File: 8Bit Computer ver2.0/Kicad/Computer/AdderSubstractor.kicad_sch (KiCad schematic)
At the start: 15 parts, among them IC140 SN74AHC74DR, IC141 SN74HCS4075DR, IC142 SN74LVC1G32DBVR, IC143 SN74AHC86DR, IC144 SN74LVC1G08DBVR, IC145 SN74LVC1G14DBVR, IC146 SN74AHC86DR, IC147 SN74ABT245BDWR, IC148 SN74F283D, IC149 SN74F283D, IC150 SN74F283D, IC151 SN74LVC1G86DBVR, IC152 SN74ABT574ADWR, IC153 SN74ABT574ADWR, IC154 SN74LVC1G14DBVR

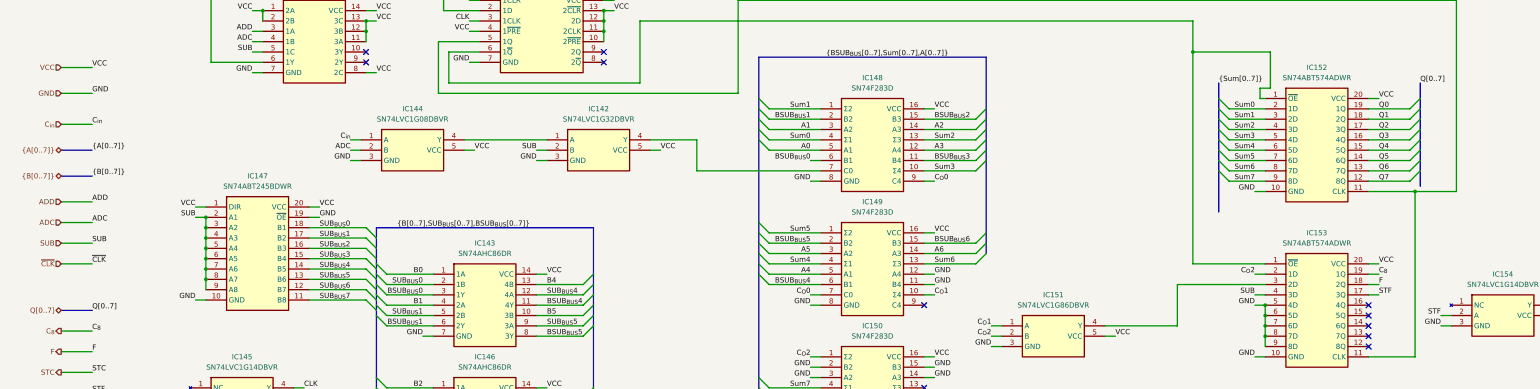
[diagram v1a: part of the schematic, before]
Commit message: Kicad, parts
Parts:
added Leds
Kicad:
added Input Output
changed Q bus to DAT bus
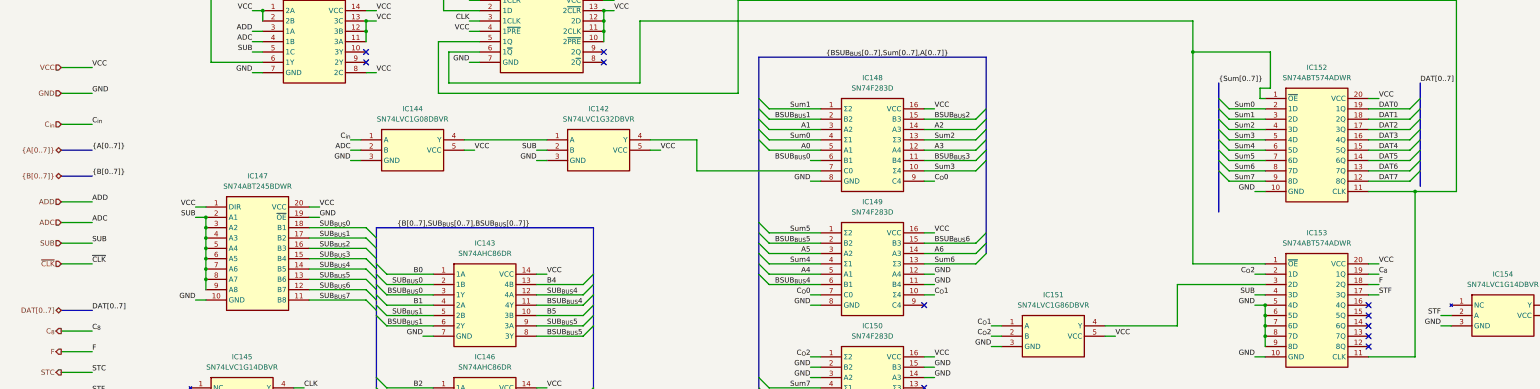
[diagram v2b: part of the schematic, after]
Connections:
- net Q0 renamed DAT0
- net Q1 renamed DAT1
- net Q2 renamed DAT2
- net Q3 renamed DAT3
- net Q4 renamed DAT4
- net Q5 renamed DAT5
- net Q6 renamed DAT6
- net Q7 renamed DAT7
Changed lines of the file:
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@@
 		)
 	)
-	(label "Q2"
+	(label "DAT2"
 		(at 355.6 64.77 0)
 		(effects
@@
 		)
 	)
-	(label "Q[0..7]"
+	(label "DAT[0..7]"
 		(at 39.37 109.22 0)
 		(effects
@@
 		)
 	)
-	(label "Q3"
+	(label "DAT3"
 		(at 355.6 67.31 0)
 		(effects
@@
 		)
 	)
-	(label "Q4"
+	(label "DAT4"
 		(at 355.6 69.85 0)
 		(effects
@@
 		)
 	)
-	(label "Q5"
+	(label "DAT5"
 		(at 355.6 72.39 0)
 		(effects
@@
 		)
 	)
-	(label "Q1"
+	(label "DAT1"
 		(at 355.6 62.23 0)
 		(effects
@@
 		)
 	)
-	(label "Q6"
+	(label "DAT6"
 		(at 355.6 74.93 0)
 		(effects
@@
 		)
 	)
-	(label "Q0"
+	(label "DAT0"
 		(at 355.6 59.69 0)
 		(effects
@@
 		)
 	)
-	(label "Q[0..7]"
+	(label "DAT[0..7]"
 		(at 365.76 53.34 0)
 		(effects
@@
 		)
 	)
-	(label "Q7"
+	(label "DAT7"
 		(at 355.6 77.47 0)
 		(effects
@@
 		)
 	)
-	(hierarchical_label "Q[0..7]"
+	(hierarchical_label "DAT[0..7]"
 		(shape tri_state)
 		(at 31.75 109.22 180)

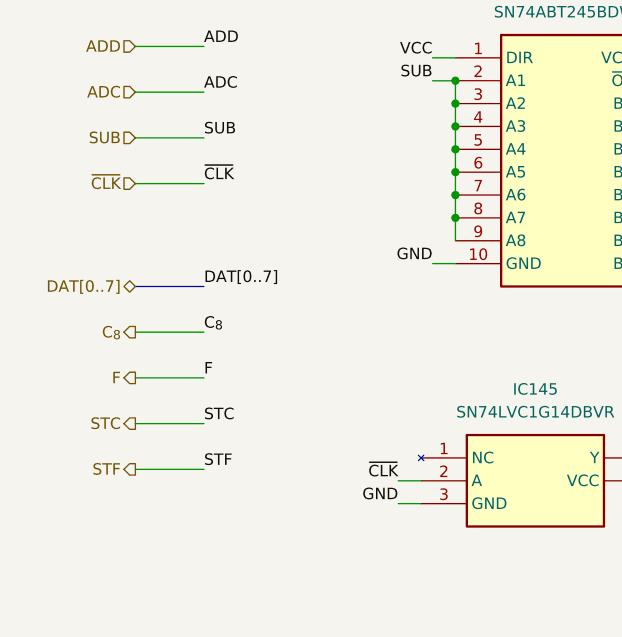
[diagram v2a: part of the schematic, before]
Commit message: Kicad, parts
parts:
added USB C PD Triggerboard
added Delay Chip for 90ns
added Push Button
Kicad:
added USB C PD Triggerboard
added rising edge detector via Delay and Xor for Accept Push Button
added VBUS net
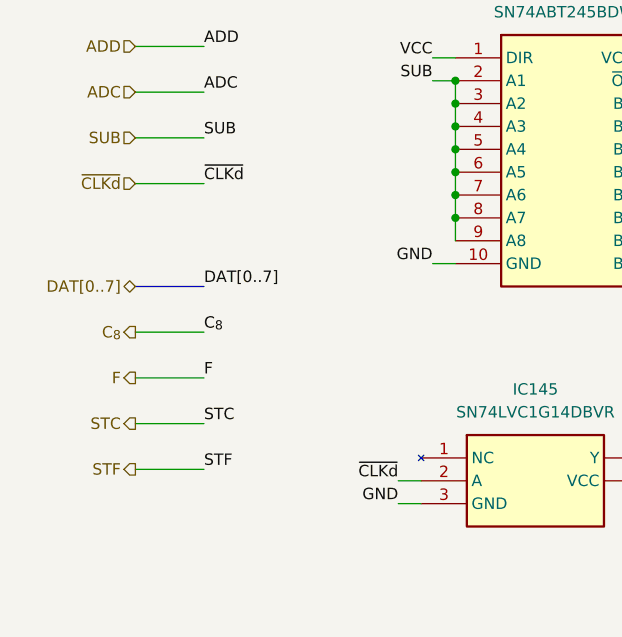
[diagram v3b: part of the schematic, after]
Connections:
- net ~{CLK} renamed ~{CLKd}
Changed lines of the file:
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@@
 		)
 	)
-	(label "~{CLK}"
+	(label "~{CLKd}"
 		(at 39.37 97.79 0)
 		(effects
@@
 		)
 	)
-	(label "~{CLK}"
+	(label "~{CLKd}"
 		(at 60.96 130.81 180)
 		(effects
@@
 		)
 	)
-	(hierarchical_label "~{CLK}"
+	(hierarchical_label "~{CLKd}"
 		(shape input)
 		(at 31.75 97.79 180)

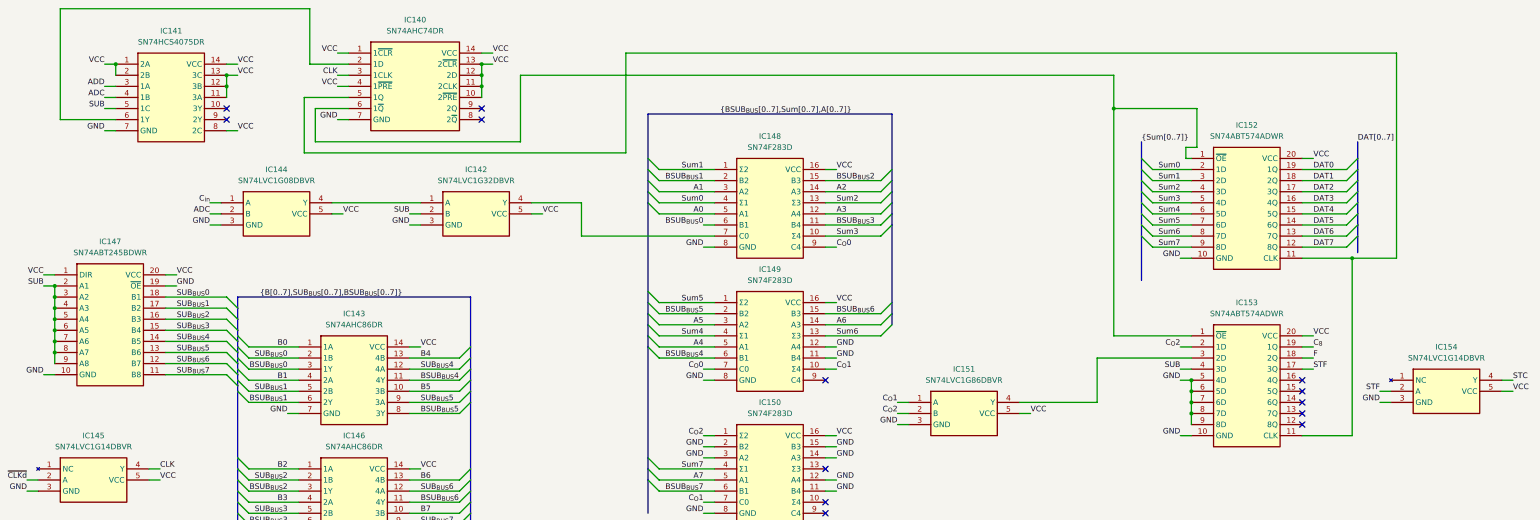
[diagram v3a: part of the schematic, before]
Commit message: Kicad SCH/PCB
Kicad SCH/PCB:
changed the References in SCH
began with INOUTPUT module nearly done
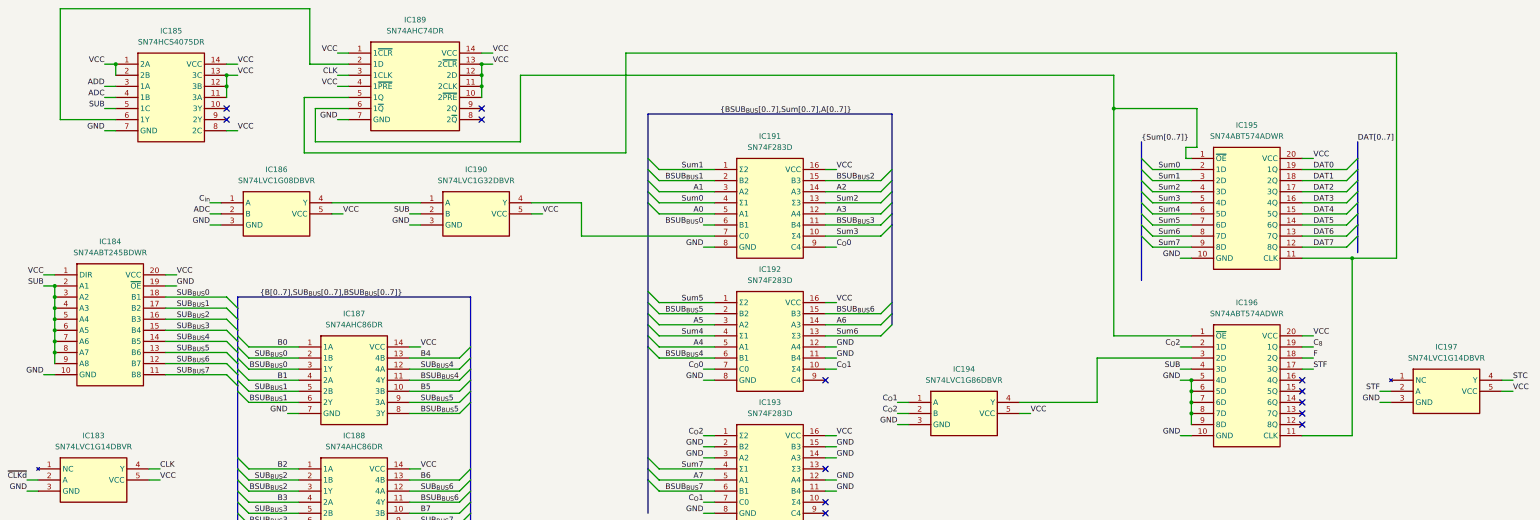
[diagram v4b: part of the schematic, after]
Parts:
- renumbered IC145 to IC183, IC147 to IC184, IC141 to IC185, IC144 to IC186, IC143 to IC187, IC146 to IC188, IC140 to IC189, IC142 to IC190, IC148 to IC191, IC149 to IC192, IC150 to IC193, IC151 to IC194, IC152 to IC195, IC153 to IC196, IC154 to IC197
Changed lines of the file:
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@@
 		(dnp no)
 		(fields_autoplaced yes)
-		(property "Reference" "IC147"
+		(property "Reference" "IC184"
 			(at 80.01 76.2 0)
 			(effects
@@
 			(project ""
 				(path "/1196a00e-6878-4d6d-82b7-9e052dfe7c14/c4d8b530-1c6d-45af-88d2-7dc1d4321a34/fab3b598-6285-4b88-9c97-383a6e59f4fc"
-					(reference "IC147")
+					(reference "IC184")
 					(unit 1)
 				)
@@
 		(dnp no)
 		(fields_autoplaced yes)
-		(property "Reference" "IC146"
+		(property "Reference" "IC188"
 			(at 135.89 120.65 0)
 			(effects
@@
 			(project "Computer"
 				(path "/1196a00e-6878-4d6d-82b7-9e052dfe7c14/c4d8b530-1c6d-45af-88d2-7dc1d4321a34/fab3b598-6285-4b88-9c97-383a6e59f4fc"
-					(reference "IC146")
+					(reference "IC188")
 					(unit 1)
 				)
@@
 		(dnp no)
 		(fields_autoplaced yes)
-		(property "Reference" "IC152"
+		(property "Reference" "IC195"
 			(at 340.36 49.53 0)
 			(effects
@@
 			(project "Computer"
 				(path "/1196a00e-6878-4d6d-82b7-9e052dfe7c14/c4d8b530-1c6d-45af-88d2-7dc1d4321a34/fab3b598-6285-4b88-9c97-383a6e59f4fc"
-					(reference "IC152")
+					(reference "IC195")
 					(unit 1)
 				)
@@
 		(dnp no)
 		(fields_autoplaced yes)
-		(property "Reference" "IC153"
+		(property "Reference" "IC196"
 			(at 340.36 90.17 0)
 			(effects
@@
 			(project "Computer"
 				(path "/1196a00e-6878-4d6d-82b7-9e052dfe7c14/c4d8b530-1c6d-45af-88d2-7dc1d4321a34/fab3b598-6285-4b88-9c97-383a6e59f4fc"
-					(reference "IC153")
+					(reference "IC196")
 					(unit 1)
 				)
@@
 		(dnp no)
 		(fields_autoplaced yes)
-		(property "Reference" "IC145"
+		(property "Reference" "IC183"
 			(at 76.2 120.65 0)
 			(effects
@@
 			(project ""
 				(path "/1196a00e-6878-4d6d-82b7-9e052dfe7c14/c4d8b530-1c6d-45af-88d2-7dc1d4321a34/fab3b598-6285-4b88-9c97-383a6e59f4fc"
-					(reference "IC145")
+					(reference "IC183")
 					(unit 1)
 				)
@@
 		(dnp no)
 		(fields_autoplaced yes)
-		(property "Reference" "IC151"
+		(property "Reference" "IC194"
 			(at 275.59 105.41 0)
 			(effects
@@
 			(project "Computer"
 				(path "/1196a00e-6878-4d6d-82b7-9e052dfe7c14/c4d8b530-1c6d-45af-88d2-7dc1d4321a34/fab3b598-6285-4b88-9c97-383a6e59f4fc"
-					(reference "IC151")
+					(reference "IC194")
 					(unit 1)
 				)
@@
 		(dnp no)
 		(fields_autoplaced yes)
-		(property "Reference" "IC149"
+		(property "Reference" "IC192"
 			(at 231.14 82.55 0)
 			(effects
@@
 			(project "Computer"
 				(path "/1196a00e-6878-4d6d-82b7-9e052dfe7c14/c4d8b530-1c6d-45af-88d2-7dc1d4321a34/fab3b598-6285-4b88-9c97-383a6e59f4fc"
-					(reference "IC149")
+					(reference "IC192")
 					(unit 1)
 				)
@@
 		(dnp no)
 		(fields_autoplaced yes)
-		(property "Reference" "IC148"
+		(property "Reference" "IC191"
 			(at 231.14 52.07 0)
 			(effects
@@
 			(project "Computer"
 				(path "/1196a00e-6878-4d6d-82b7-9e052dfe7c14/c4d8b530-1c6d-45af-88d2-7dc1d4321a34/fab3b598-6285-4b88-9c97-383a6e59f4fc"
-					(reference "IC148")
+					(reference "IC191")
 					(unit 1)
 				)
@@
 		(dnp no)
 		(fields_autoplaced yes)
-		(property "Reference" "IC142"
+		(property "Reference" "IC190"
 			(at 163.83 59.69 0)
 			(effects
@@
 			(project ""
 				(path "/1196a00e-6878-4d6d-82b7-9e052dfe7c14/c4d8b530-1c6d-45af-88d2-7dc1d4321a34/fab3b598-6285-4b88-9c97-383a6e59f4fc"
-					(reference "IC142")
+					(reference "IC190")
 					(unit 1)
 				)
@@
 		(dnp no)
 		(fields_autoplaced yes)
-		(property "Reference" "IC140"
+		(property "Reference" "IC189"
 			(at 149.86 25.4 0)
 			(effects
@@
 			(project ""
 				(path "/1196a00e-6878-4d6d-82b7-9e052dfe7c14/c4d8b530-1c6d-45af-88d2-7dc1d4321a34/fab3b598-6285-4b88-9c97-383a6e59f4fc"
-					(reference "IC140")
+					(reference "IC189")
 					(unit 1)
 				)
@@
 		(dnp no)
 		(fields_autoplaced yes)
-		(property "Reference" "IC141"
+		(property "Reference" "IC185"
 			(at 93.98 27.94 0)
 			(effects
@@
 			(project ""
 				(path "/1196a00e-6878-4d6d-82b7-9e052dfe7c14/c4d8b530-1c6d-45af-88d2-7dc1d4321a34/fab3b598-6285-4b88-9c97-383a6e59f4fc"
-					(reference "IC141")
+					(reference "IC185")
 					(unit 1)
 				)
@@
 		(dnp no)
 		(fields_autoplaced yes)
-		(property "Reference" "IC144"
+		(property "Reference" "IC186"
 			(at 118.11 59.69 0)
 			(effects
@@
 			(project ""
 				(path "/1196a00e-6878-4d6d-82b7-9e052dfe7c14/c4d8b530-1c6d-45af-88d2-7dc1d4321a34/fab3b598-6285-4b88-9c97-383a6e59f4fc"
-					(reference "IC144")
+					(reference "IC186")
 					(unit 1)
 				)
@@
 		(dnp no)
 		(fields_autoplaced yes)
-		(property "Reference" "IC150"
+		(property "Reference" "IC193"
 			(at 231.14 113.03 0)
 			(effects
@@
 			(project "Computer"
 				(path "/1196a00e-6878-4d6d-82b7-9e052dfe7c14/c4d8b530-1c6d-45af-88d2-7dc1d4321a34/fab3b598-6285-4b88-9c97-383a6e59f4fc"
-					(reference "IC150")
+					(reference "IC193")
 					(unit 1)
 				)
@@
 		(dnp no)
 		(fields_autoplaced yes)
-		(property "Reference" "IC154"
+		(property "Reference" "IC197"
 			(at 386.08 100.33 0)
 			(effects
@@
 			(project ""
 				(path "/1196a00e-6878-4d6d-82b7-9e052dfe7c14/c4d8b530-1c6d-45af-88d2-7dc1d4321a34/fab3b598-6285-4b88-9c97-383a6e59f4fc"
-					(reference "IC154")
+					(reference "IC197")
 					(unit 1)
 				)
@@
 		(dnp no)
 		(fields_autoplaced yes)
-		(property "Reference" "IC143"
+		(property "Reference" "IC187"
 			(at 135.89 92.71 0)
 			(effects
@@
 			(project ""
 				(path "/1196a00e-6878-4d6d-82b7-9e052dfe7c14/c4d8b530-1c6d-45af-88d2-7dc1d4321a34/fab3b598-6285-4b88-9c97-383a6e59f4fc"
-					(reference "IC143")
+					(reference "IC187")
 					(unit 1)
 				)
